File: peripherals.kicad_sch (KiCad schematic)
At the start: 0 parts

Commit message: peripherals finished
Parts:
- added C12, C13, C14: 0.1uF, symbol Device:C
- added J2: PPTC061LFBN-RC, PPTC061LFBN-RC:SULLINS_PPTC061LFBN-RC, symbol KeyboardSymbols:PPTC061LFBN-RC
- added SW1: RotaryEncoder_Switch_MP, symbol Device:RotaryEncoder_Switch_MP
- added U4: AT24C32E-SSHM-T, 8S1_MCH, symbol KeyboardSymbols:AT24C32E-SSHM-T
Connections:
- new net +3.3V: C12.1, J2.1, U4.8 (VCC)
- new net EEPROM_SCL: U4.6 (SCL)
- new net EEPROM_SDA: U4.5 (SDA)
- new net ENC_A: C13.2, SW1.A
- new net ENC_B: C14.1, SW1.B
- new net ENC_SW: SW1.S1
- new net GND: C12.2, C13.1, C14.2, J2.2, SW1.C, SW1.MP, SW1.S2, U4.1 (A0), U4.2 (A1), U4.3 (A2), U4.4 (GND), U4.7 (WP)
- new net SCREEN_CS: J2.6
- new net SCREEN_DS: J2.5
- new net SCREEN_SCL: J2.3
- new net SCREEN_SDA: J2.4

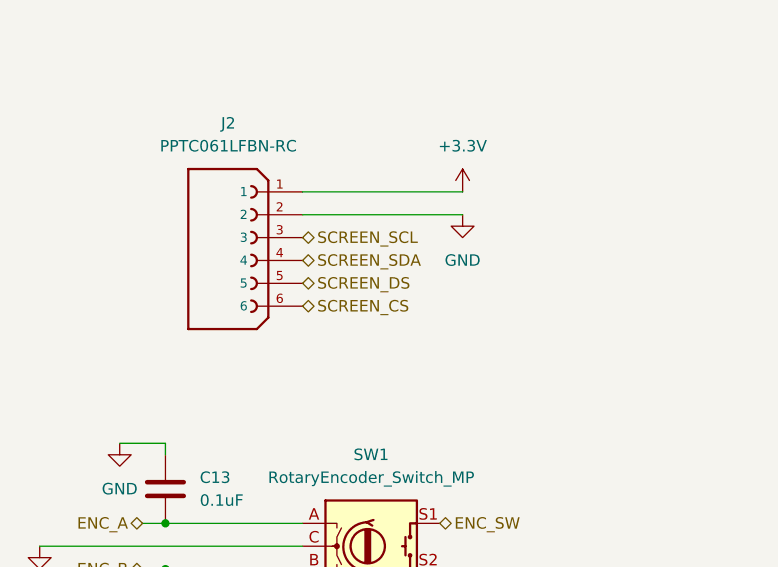
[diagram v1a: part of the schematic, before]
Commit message: switch matrix set-up
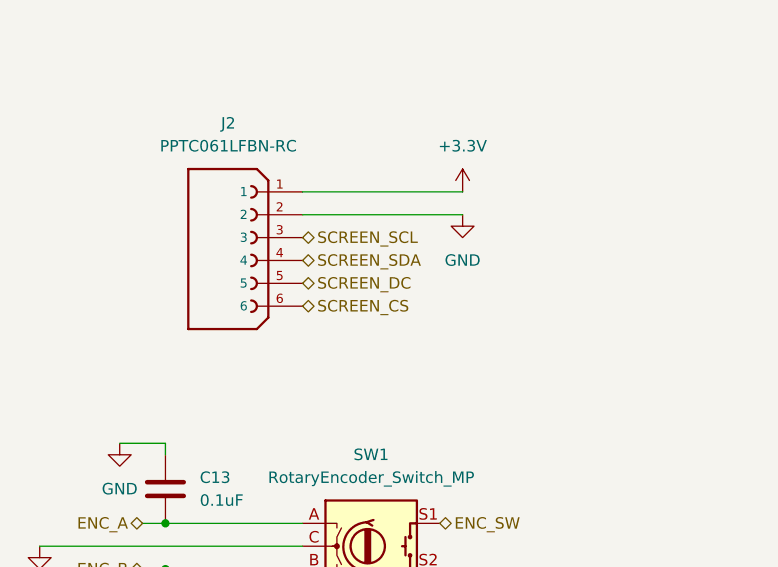
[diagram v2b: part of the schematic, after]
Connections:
- net SCREEN_DS renamed SCREEN_DC
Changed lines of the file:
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@@
 		)
 	)
-	(hierarchical_label "SCREEN_DS"
+	(hierarchical_label "SCREEN_DC"
 		(shape bidirectional)
 		(at 59.69 85.09 0)
@@
 				)
 			)
+			(project "peripherals"
+				(path "/f65e89d2-9291-492e-b58a-1f98bb831d95"
+					(reference "#PWR029")
+					(unit 1)
+				)
+			)
 		)
 	)
@@
 				)
 			)
+			(project "peripherals"
+				(path "/f65e89d2-9291-492e-b58a-1f98bb831d95"
+					(reference "C12")
+					(unit 1)
+				)
+			)
 		)
 	)
@@
 				)
 			)
+			(project "peripherals"
+				(path "/f65e89d2-9291-492e-b58a-1f98bb831d95"
+					(reference "U4")
+					(unit 1)
+				)
+			)
 		)
 	)
@@
 				)
 			)
+			(project "peripherals"
+				(path "/f65e89d2-9291-492e-b58a-1f98bb831d95"
+					(reference "#PWR030")
+					(unit 1)
+				)
+			)
 		)
 	)
@@
 				)
 			)
+			(project "peripherals"
+				(path "/f65e89d2-9291-492e-b58a-1f98bb831d95"
+					(reference "C13")
+					(unit 1)
+				)
+			)
 		)
 	)
@@
 				)
 			)
+			(project "peripherals"
+				(path "/f65e89d2-9291-492e-b58a-1f98bb831d95"
+					(reference "#PWR024")
+					(unit 1)
+				)
+			)
 		)
 	)
@@
 				)
 			)
+			(project "peripherals"
+				(path "/f65e89d2-9291-492e-b58a-1f98bb831d95"
+					(reference "#PWR028")
+					(unit 1)
+				)
+			)
 		)
 	)
@@
 				)
 			)
+			(project "peripherals"
+				(path "/f65e89d2-9291-492e-b58a-1f98bb831d95"
+					(reference "#PWR025")
+					(unit 1)
+				)
+			)
 		)
 	)
@@
 				)
 			)
+			(project "peripherals"
+				(path "/f65e89d2-9291-492e-b58a-1f98bb831d95"
+					(reference "J2")
+					(unit 1)
+				)
+			)
 		)
 	)
@@
 				)
 			)
+			(project "peripherals"
+				(path "/f65e89d2-9291-492e-b58a-1f98bb831d95"
+					(reference "#PWR020")
+					(unit 1)
+				)
+			)
 		)
 	)
@@
 				)
 			)
+			(project "peripherals"
+				(path "/f65e89d2-9291-492e-b58a-1f98bb831d95"
+					(reference "#PWR022")
+					(unit 1)
+				)
+			)
 		)
 	)
@@
 				)
 			)
+			(project "peripherals"
+				(path "/f65e89d2-9291-492e-b58a-1f98bb831d95"
+					(reference "SW1")
+					(unit 1)
+				)
+			)
 		)
 	)
@@
 				)
 			)
+			(project "peripherals"
+				(path "/f65e89d2-9291-492e-b58a-1f98bb831d95"
+					(reference "#PWR019")
+					(unit 1)
+				)
+			)
 		)
 	)
@@
 				)
 			)
+			(project "peripherals"
+				(path "/f65e89d2-9291-492e-b58a-1f98bb831d95"
+					(reference "#PWR026")
+					(unit 1)
+				)
+			)
 		)
 	)
@@
 			(project "octo_keyboard"
 				(path "/e2f6b5f5-4c68-42ad-a343-f16c1cb3ab86/735cb541-7b7a-461f-b38e-cddf54100f29"
+					(reference "C14")
+					(unit 1)
+				)
+			)
+			(project "peripherals"
+				(path "/f65e89d2-9291-492e-b58a-1f98bb831d95"
 					(reference "C14")
 					(unit 1)
@@
 				)
 			)
+			(project "peripherals"
+				(path "/f65e89d2-9291-492e-b58a-1f98bb831d95"
+					(reference "#PWR021")
+					(unit 1)
+				)
+			)
 		)
 	)
@@
 				)
 			)
-		)
-	)
+			(project "peripherals"
+				(path "/f65e89d2-9291-492e-b58a-1f98bb831d95"
+					(reference "#PWR027")
+					(unit 1)
+				)
+			)
+		)
+	)
+	(sheet_instances
+		(path "/"
+			(page "1")
+		)
+	)
+	(embedded_fonts no)
 )

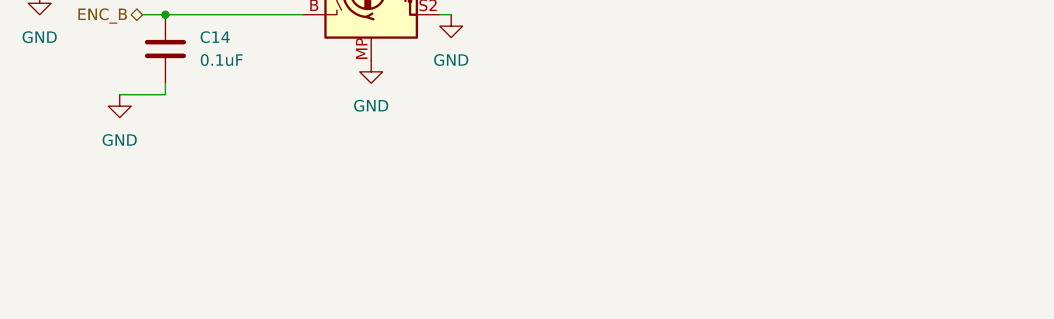
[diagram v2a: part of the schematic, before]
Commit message: cleaned up top-level connections
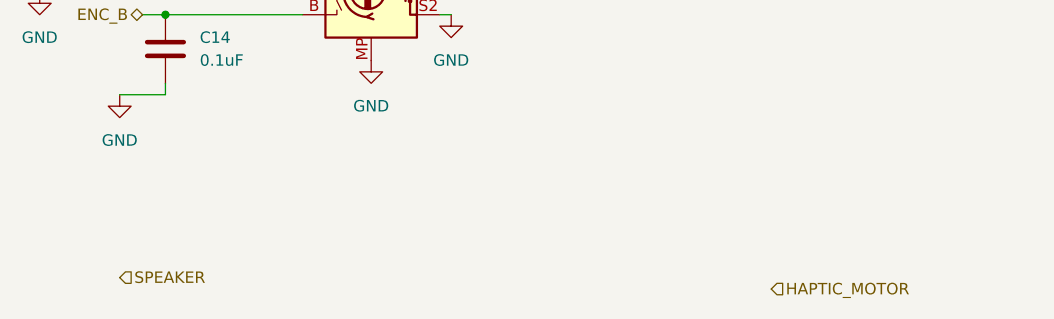
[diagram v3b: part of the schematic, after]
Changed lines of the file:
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@@
+		)
+	)
+	(hierarchical_label "SPEAKER"
+		(shape input)
+		(at 39.37 146.05 0)
+		(effects
+			(font
+				(size 1.27 1.27)
+			)
+			(justify left)
 		)
 	)
@@
 		(effects
 			(font
+				(size 1.27 1.27)
+			)
+			(justify left)
+		)
+	)
+	(hierarchical_label "HAPTIC_MOTOR"
+		(shape input)
+		(at 111.76 147.32 0)
+		(effects
+			(font

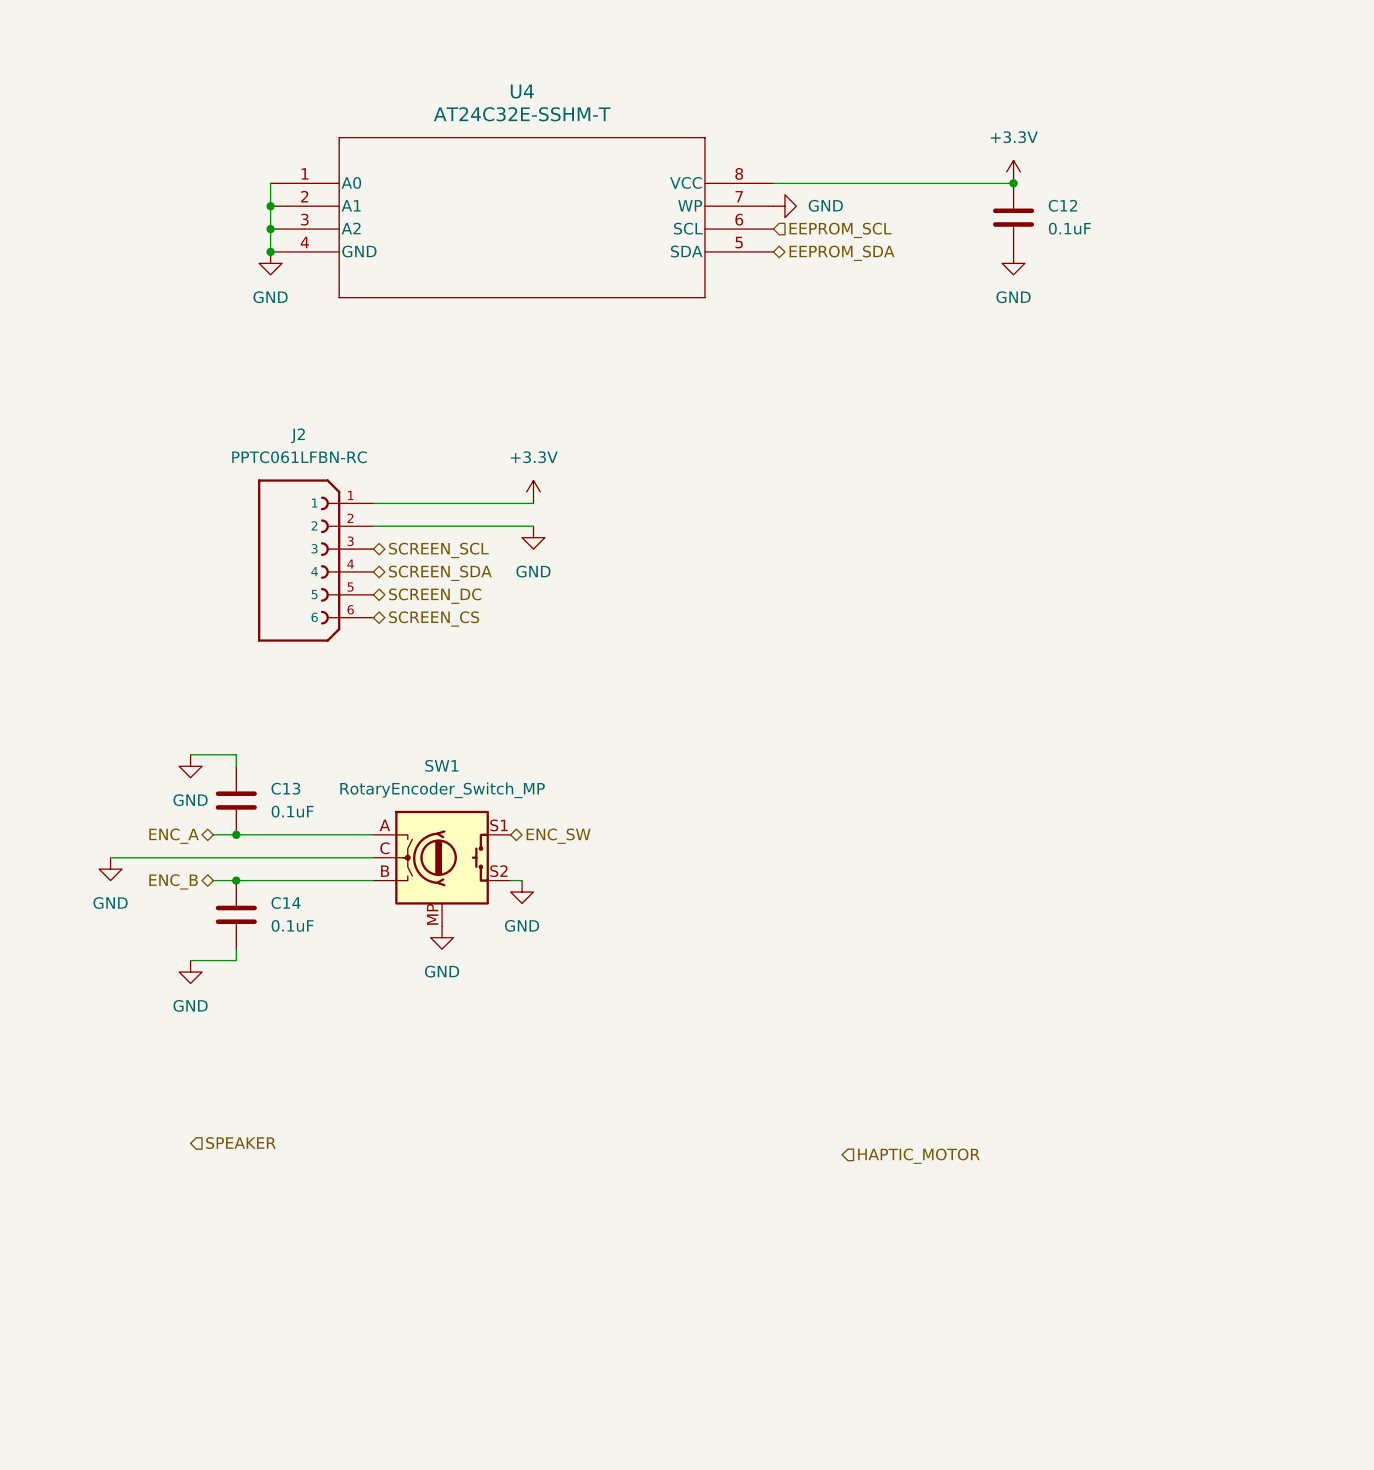
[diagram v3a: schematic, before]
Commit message: documentation for switch matrix, peripherals
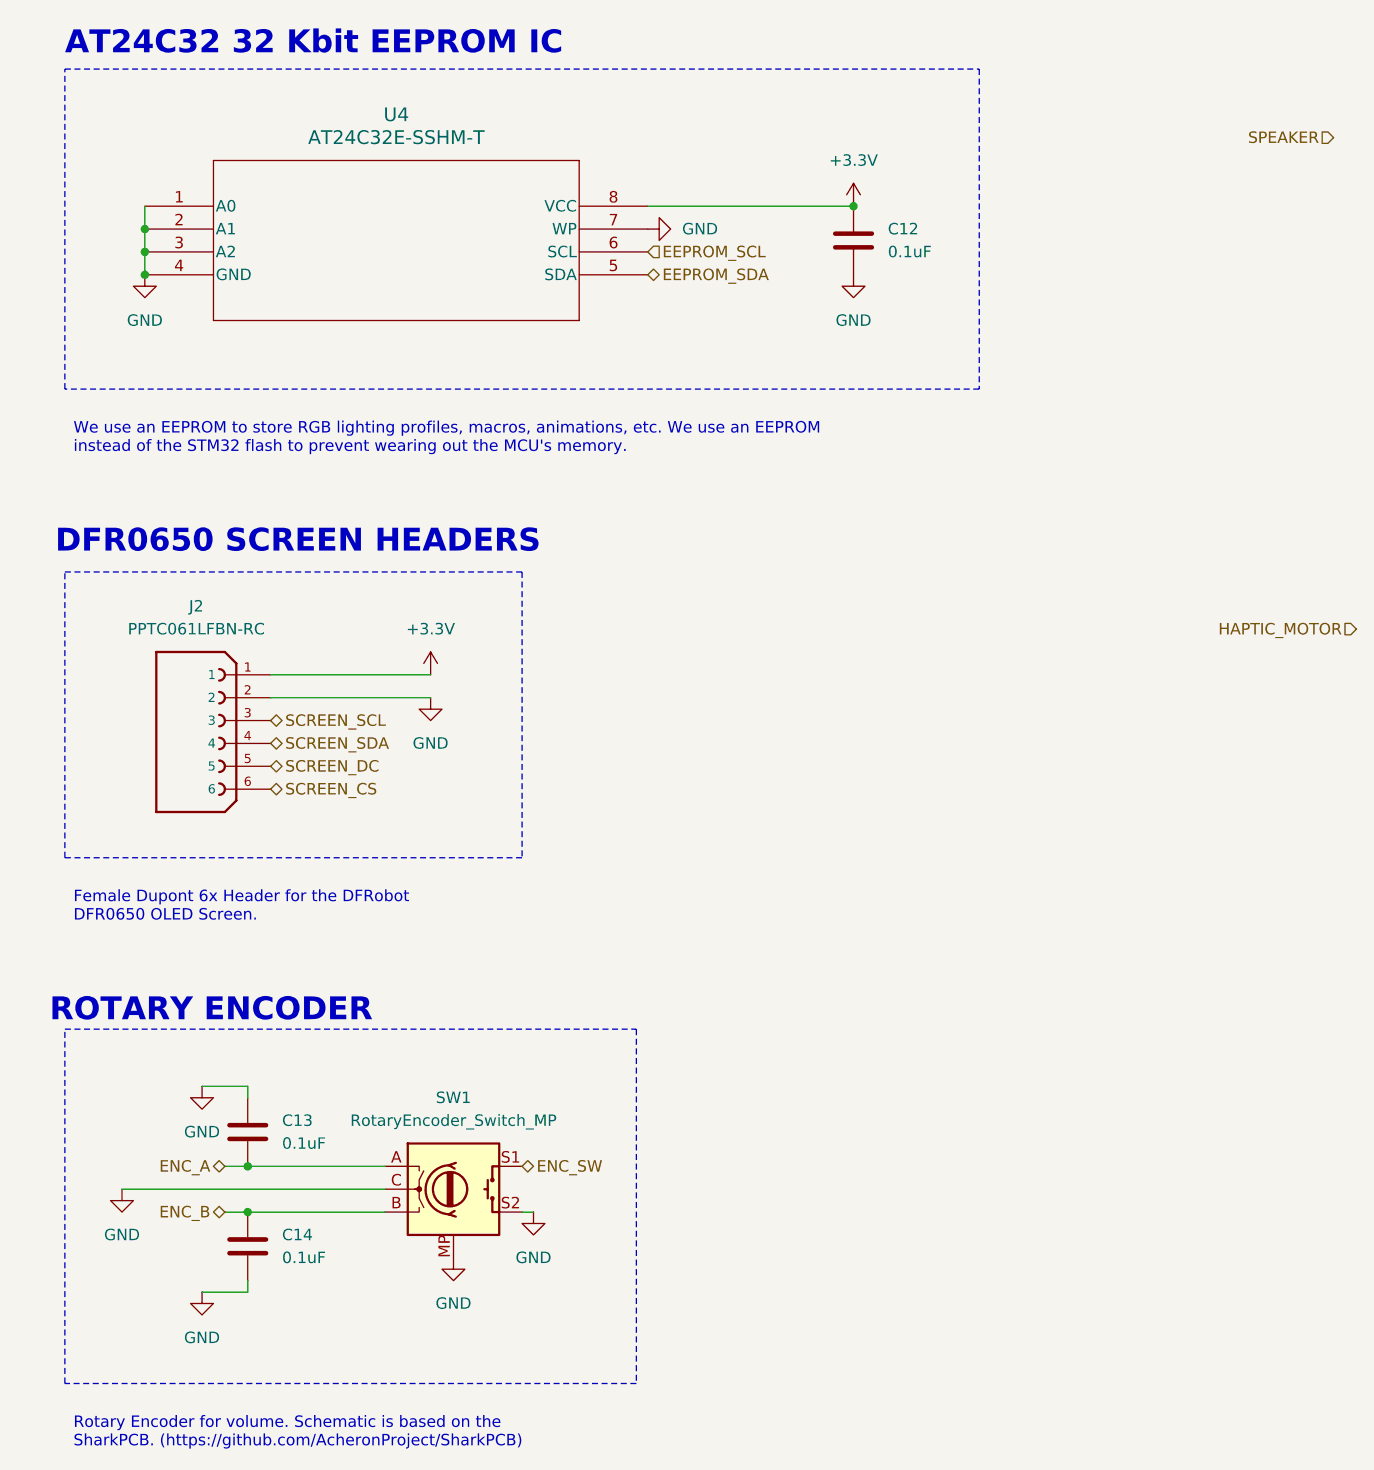
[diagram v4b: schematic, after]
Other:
- note added: "AT24C32 32 Kbit EEPROM IC"
- note added: "DFR0650 SCREEN HEADERS"
- note added: "ROTARY ENCODER"
- moved on the sheet: C12, C13, C14, J2, SW1, U4
